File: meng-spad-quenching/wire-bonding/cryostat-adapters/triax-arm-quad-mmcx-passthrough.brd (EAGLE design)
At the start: 19.1 x 44.5 mm, 8 parts, among them X1 A, X2 B, X3 C, X4 D, X5 AA, X6 BB, X7 CC, X8 DD

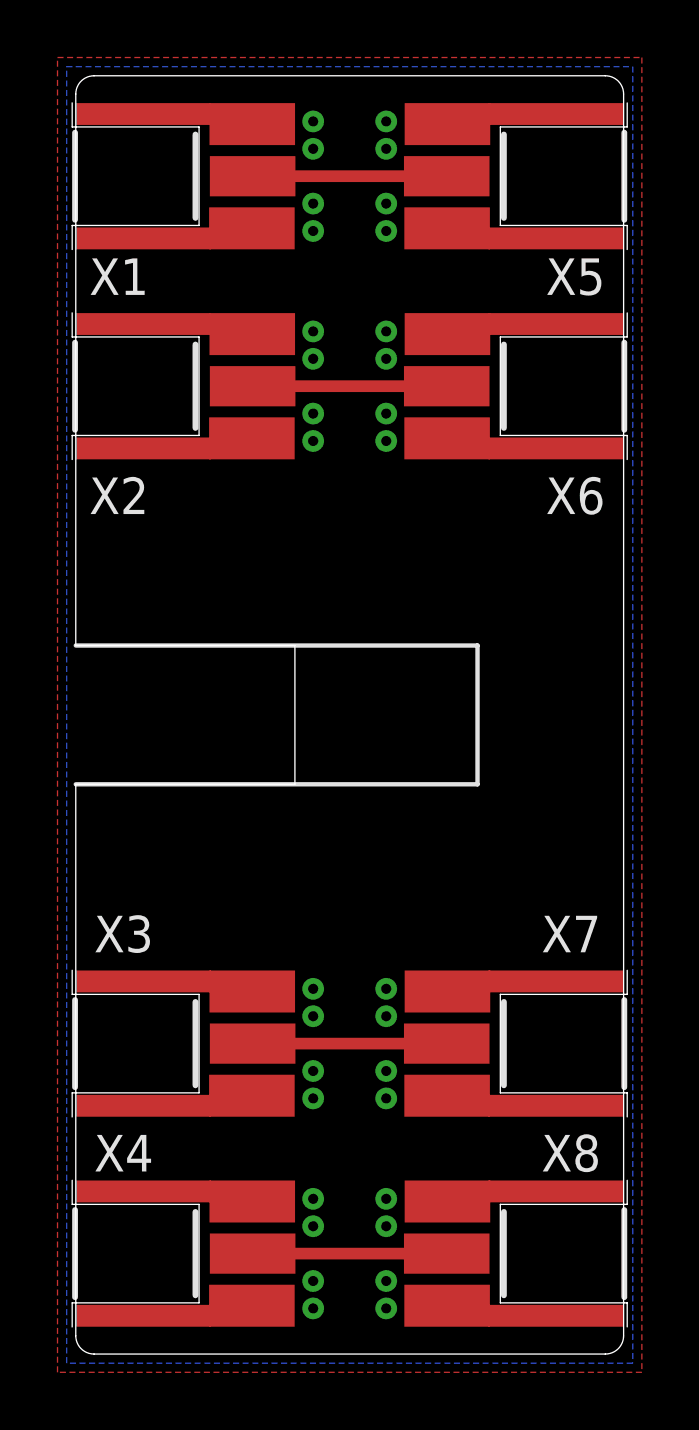
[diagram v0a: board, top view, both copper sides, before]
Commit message: Modified leaf-heater and triax-passthrough for second sendout
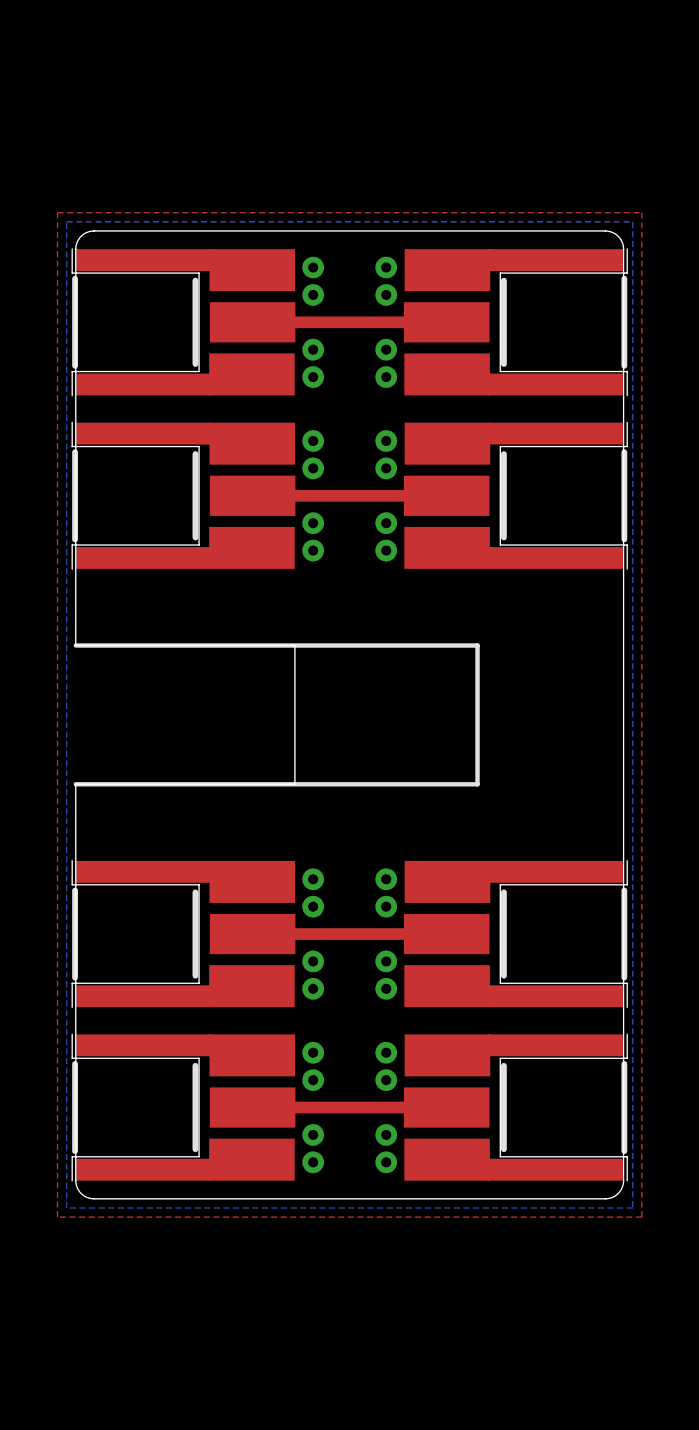
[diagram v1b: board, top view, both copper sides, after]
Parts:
- moved X1 5.08 mm to (0.00, 13.7)
- moved X4 5.08 mm to (0.00, -13.7)
- moved X5 5.08 mm to (19.1, 13.7)
- moved X8 5.08 mm to (19.1, -13.7)
- moved X2 3.81 mm to (0.00, 7.62)
- moved X3 3.81 mm to (0.00, -7.62)
- moved X6 3.81 mm to (19.1, 7.62)
- moved X7 3.81 mm to (19.1, -7.62)
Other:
- board size 19.1 x 44.5 mm -> 19.1 x 33.7 mm

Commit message: Updates to component selection
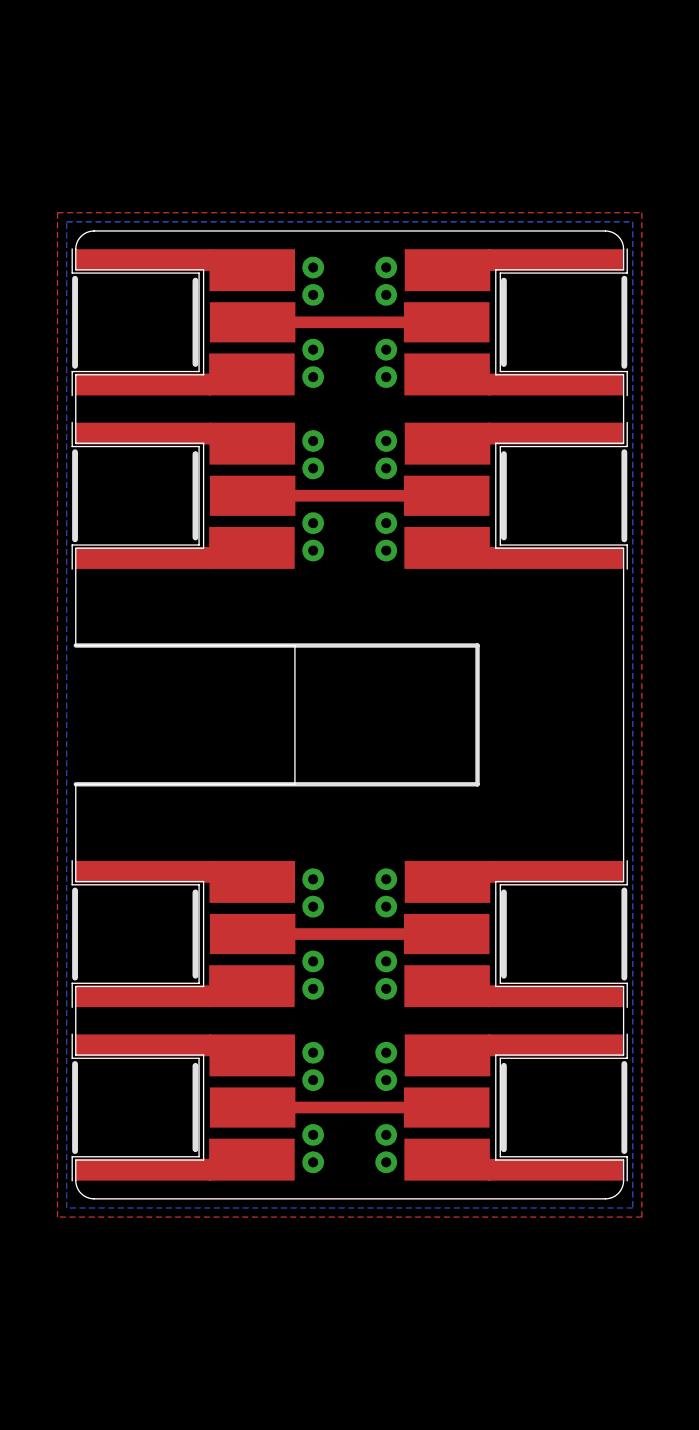
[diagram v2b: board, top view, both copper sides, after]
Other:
- outline, holes or cut-outs redrawn
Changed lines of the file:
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@@
 <setting verticaltext="up"/>
 </settings>
-<grid distance="0.0125" unitdist="inch" unit="inch" style="lines" multiple="1" display="yes" altdistance="5" altunitdist="mil" altunit="mil"/>
+<grid distance="3.125" unitdist="mil" unit="mil" style="lines" multiple="1" display="yes" altdistance="5" altunitdist="mil" altunit="mil"/>
 <layers>
 <layer number="1" name="Top" color="4" fill="1" visible="yes" active="yes"/>
@@
 <wire x1="0.635" y1="-16.8275" x2="18.415" y2="-16.8275" width="0" layer="20"/>
 <wire x1="18.415" y1="-16.8275" x2="19.05" y2="-16.1925" width="0" layer="20" curve="90"/>
-<wire x1="19.05" y1="-16.1925" x2="19.05" y2="16.1925" width="0" layer="20"/>
+<wire x1="19.05" y1="-16.1925" x2="19.05" y2="-15.478125" width="0" layer="20"/>
+<wire x1="19.05" y1="-15.478125" x2="14.605" y2="-15.478125" width="0" layer="20"/>
+<wire x1="14.605" y1="-15.478125" x2="14.605" y2="-11.826875" width="0" layer="20"/>
+<wire x1="14.605" y1="-11.826875" x2="19.05" y2="-11.826875" width="0" layer="20"/>
+<wire x1="19.05" y1="-11.826875" x2="19.05" y2="-9.445625" width="0" layer="20"/>
+<wire x1="19.05" y1="-9.445625" x2="14.605" y2="-9.445625" width="0" layer="20"/>
+<wire x1="14.605" y1="-9.445625" x2="14.605" y2="-5.794375" width="0" layer="20"/>
+<wire x1="14.605" y1="-5.794375" x2="19.05" y2="-5.794375" width="0" layer="20"/>
+<wire x1="19.05" y1="-5.794375" x2="19.05" y2="5.794375" width="0" layer="20"/>
+<wire x1="19.05" y1="5.794375" x2="14.605" y2="5.794375" width="0" layer="20"/>
+<wire x1="14.605" y1="5.794375" x2="14.605" y2="9.445625" width="0" layer="20"/>
+<wire x1="14.605" y1="9.445625" x2="19.05" y2="9.445625" width="0" layer="20"/>
+<wire x1="19.05" y1="9.445625" x2="19.05" y2="11.826875" width="0" layer="20"/>
+<wire x1="19.05" y1="11.826875" x2="14.605" y2="11.826875" width="0" layer="20"/>
+<wire x1="14.605" y1="11.826875" x2="14.605" y2="15.478125" width="0" layer="20"/>
+<wire x1="14.605" y1="15.478125" x2="19.05" y2="15.478125" width="0" layer="20"/>
+<wire x1="19.05" y1="15.478125" x2="19.05" y2="16.1925" width="0" layer="20"/>
 <wire x1="19.05" y1="16.1925" x2="18.415" y2="16.8275" width="0" layer="20" curve="90"/>
 <wire x1="18.415" y1="16.8275" x2="0.635" y2="16.8275" width="0" layer="20"/>
 <wire x1="0.635" y1="16.8275" x2="0" y2="16.1925" width="0" layer="20" curve="90"/>
-<wire x1="0" y1="16.1925" x2="0" y2="2.413" width="0" layer="20"/>
+<wire x1="0" y1="16.1925" x2="0" y2="15.478125" width="0" layer="20"/>
+<wire x1="0" y1="15.478125" x2="4.445" y2="15.478125" width="0" layer="20"/>
+<wire x1="4.445" y1="15.478125" x2="4.445" y2="11.826875" width="0" layer="20"/>
+<wire x1="4.445" y1="11.826875" x2="0" y2="11.826875" width="0" layer="20"/>
+<wire x1="0" y1="11.826875" x2="0" y2="9.445625" width="0" layer="20"/>
+<wire x1="0" y1="9.445625" x2="4.445" y2="9.445625" width="0" layer="20"/>
+<wire x1="4.445" y1="9.445625" x2="4.445" y2="5.794375" width="0" layer="20"/>
+<wire x1="4.445" y1="5.794375" x2="0" y2="5.794375" width="0" layer="20"/>
+<wire x1="0" y1="5.794375" x2="0" y2="2.413" width="0" layer="20"/>
 <wire x1="0.635" y1="-16.8275" x2="0" y2="-16.1925" width="0" layer="20" curve="-90"/>
-<wire x1="0" y1="-16.1925" x2="0" y2="-2.413" width="0" layer="20"/>
+<wire x1="0" y1="-16.1925" x2="0" y2="-15.478125" width="0" layer="20"/>
+<wire x1="0" y1="-15.478125" x2="4.445" y2="-15.478125" width="0" layer="20"/>
+<wire x1="4.445" y1="-15.478125" x2="4.445" y2="-11.826875" width="0" layer="20"/>
+<wire x1="4.445" y1="-11.826875" x2="0" y2="-11.826875" width="0" layer="20"/>
+<wire x1="0" y1="-11.826875" x2="0" y2="-9.445625" width="0" layer="20"/>
+<wire x1="0" y1="-9.445625" x2="4.445" y2="-9.445625" width="0" layer="20"/>
+<wire x1="4.445" y1="-9.445625" x2="4.445" y2="-5.794375" width="0" layer="20"/>
+<wire x1="4.445" y1="-5.794375" x2="0" y2="-5.794375" width="0" layer="20"/>
+<wire x1="0" y1="-5.794375" x2="0" y2="-2.413" width="0" layer="20"/>
 <wire x1="0" y1="2.413" x2="7.62" y2="2.413" width="0" layer="20"/>
 <wire x1="7.62" y1="2.413" x2="7.62" y2="-2.413" width="0" layer="20"/>
@@
 <param name="dpMaxLengthDifference" value="10mm"/>
 <param name="dpGapFactor" value="2.5"/>
-<param name="checkAngle" value="0"/>
+<param name="checkAngle" value="1"/>
 <param name="checkFont" value="1"/>
 <param name="checkRestrict" value="1"/>
